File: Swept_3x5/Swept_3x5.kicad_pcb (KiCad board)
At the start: 2 copper layers, 261.1 x 90.7 mm, 98 parts, among them SW10 SW_Push, SW10_r1 SW_Push, SW11 SW_Push, SW11_r1 SW_Push, SW12 SW_Push, SW12_r1 SW_Push, SW13 SW_Push, SW13_r1 SW_Push, SW14 SW_Push, SW14_r1 SW_Push, SW15 SW_Push, SW15_r1 SW_Push, SW16 SW_Push, SW16_r1 SW_Push, SW17 SW_Push, SW17_r1 SW_Push, SW18 SW_Push, SW18_r1 SW_Push, SW19 SW_Push, SW19_r1 SW_Push, SW2 SW_Push, SW20 SW_Push, SW20_r1 SW_Push, SW21 SW_Push, SW21_r1 SW_Push, SW22 SW_Push, SW22_r1 SW_Push, SW2_r1 SW_Push, SW3 SW_Push, SW3_r1 SW_Push, SW4 SW_Push, SW4_r1 SW_Push, SW5 SW_Push, SW5_r1 SW_Push, SW6 SW_Push, SW6_r1 SW_Push, SW7 SW_Push, SW7_r1 SW_Push, SW8 SW_Push, SW8_r1 SW_Push, SW9 SW_Push, SW9_r1 SW_Push, U1 ProMicro-kbd, U2 ProMicro-kbd

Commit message: Version 0.2.0
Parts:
- removed D0, D12, D6, Dr0, Dr12, Dr6: D, kbd:D3_SMD_v2
- removed SW14, SW14_r1, SW2, SW2_r1, SW8, SW8_r1: SW_Push, aym1607:choc-v1-with-millmax
- moved + 34.1 mm to (229.8, 47.6)
- moved - 34.1 mm to (241.9, 47.7)
- moved D1 34.1 mm to (141.8, 42.2)
- moved D10 34.1 mm to (195.7, 45.9)
- moved D13 34.1 mm to (141.8, 76.5)
- moved D14 34.1 mm to (159.7, 64.7)
- moved D15 34.1 mm to (177.8, 57.6)
- moved D16 34.1 mm to (195.7, 63.0)
- moved D18 34.1 mm to (194.5, 92.5)
- moved D19 34.1 mm to (213.2, 94.9)
- moved D2 34.1 mm to (159.8, 30.2)
- moved D3 34.1 mm to (177.8, 23.4)
- moved D4 34.1 mm to (195.8, 28.8)
- moved D7 34.1 mm to (141.6, 59.3)
- moved D8 34.1 mm to (159.8, 47.4)
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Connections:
- U1 pad 20: col0 -> unconnected-(U1-Pad20)
- U2 pad 20: col0r -> unconnected-(U2-Pad20)
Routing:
- net col0r: track 186.0 -> 0.00 mm, vias 3 -> 0
- net col0: track 162.3 -> 0.00 mm, vias 3 -> 0
- net row_2: track 171.9 -> 150.8 mm
- net row_2r: track 135.4 -> 114.8 mm
- net row_1r: track 148.3 -> 127.8 mm
- net row_0r: track 174.3 -> 154.3 mm
- net row_0: track 213.1 -> 193.2 mm
- net row_1: track 188.3 -> 168.5 mm
- net Net-(Dr0-Pad2): track 15.9 -> 0.00 mm
- net Net-(SW8_r1-Pad2): track 15.8 -> 0.00 mm
- net Net-(Dr12-Pad2): track 15.3 -> 0.00 mm
- net Net-(D0-Pad2): track 9.28 -> 0.00 mm
- net Net-(D6-Pad2): track 9.07 -> 0.00 mm
- net Net-(D12-Pad2): track 8.91 -> 0.00 mm
- net Net-(Dr18-Pad2): track 17.3 -> 10.6 mm
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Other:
- board size 261.1 x 90.7 mm -> 227.1 x 91 mm

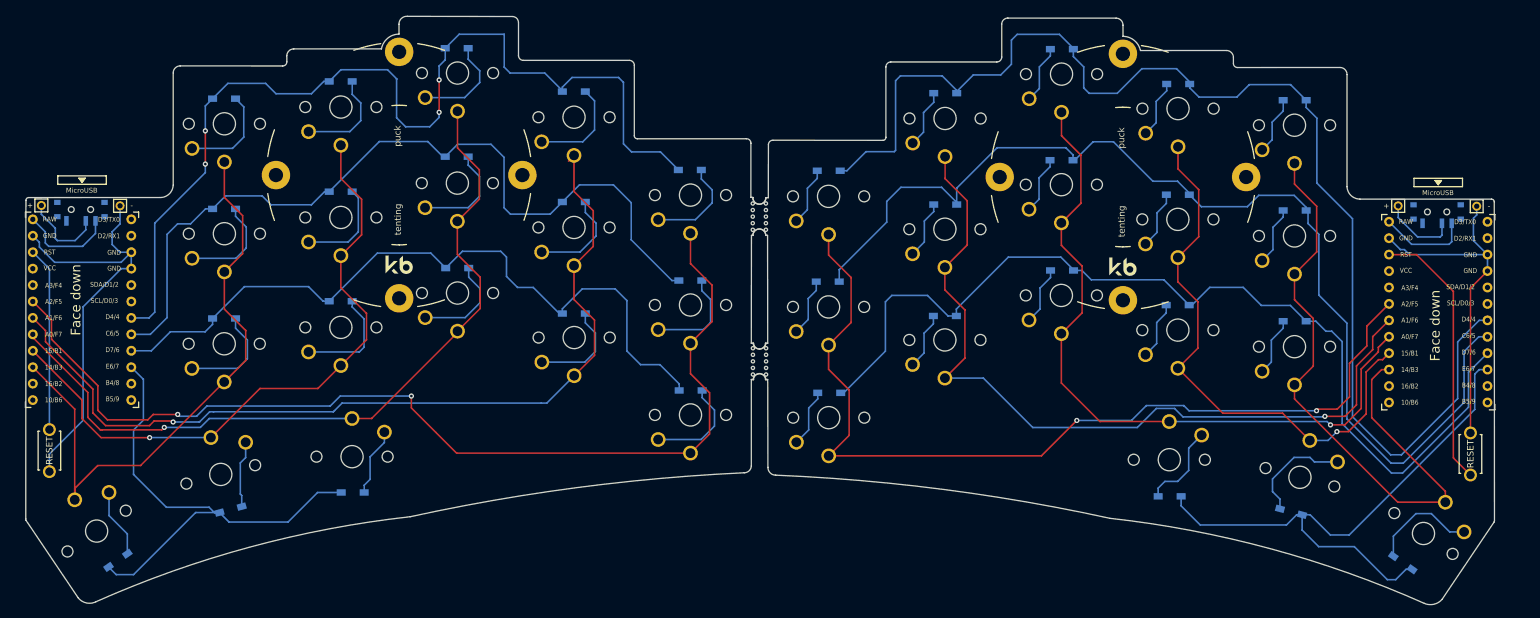
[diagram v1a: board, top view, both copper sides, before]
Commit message: Added support for Kailh hot-swap sockets.
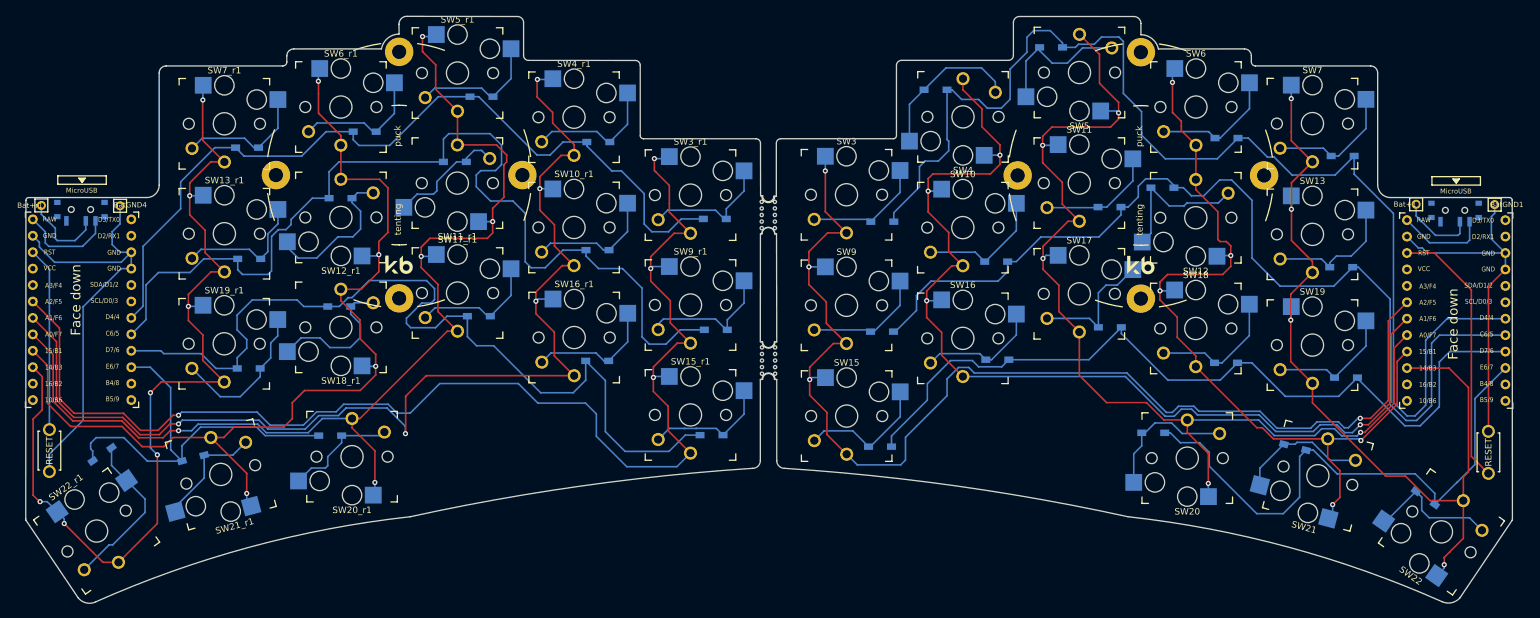
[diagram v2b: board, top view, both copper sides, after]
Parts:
- SW10, SW10_r1, SW11, SW11_r1, SW12, SW12_r1, SW13, SW13_r1, SW15, SW15_r1, SW16, SW16_r1, SW17, SW17_r1, SW18, SW18_r1, SW19, SW19_r1, SW20, SW20_r1, SW21, SW21_r1, SW22, SW22_r1, SW3, SW3_r1, SW4, SW4_r1, SW5, SW5_r1, SW6, SW6_r1, SW7, SW7_r1, SW9, SW9_r1: footprint aym1607:choc-v1-with-millmax -> keyswitches:Kailh_socket_PG1350_optional
- moved Dr20 16.6 mm to (29.4, 86.1)
- moved D8 11.8 mm to (167.7, 56.3)
- moved D17 11.8 mm to (221.7, 74.2)
- moved D16 11.6 mm to (203.2, 71.9)
- moved D15 11.5 mm to (185.2, 66.4)
- moved D13 11.4 mm to (149.7, 84.9)
- moved D1 11.4 mm to (150.1, 50.1)
- moved D7 11.4 mm to (150.0, 67.1)
- moved D5 11.4 mm to (221.2, 39.9)
- moved D11 11.3 mm to (221.0, 57.1)
- moved D4 11.2 mm to (203.3, 37.2)
- moved D20 10.6 mm to (234.0, 92.8)
- moved D14 10.6 mm to (167.8, 71.4)
- moved D9 10.4 mm to (185.2, 47.8)
- moved D18 10.1 mm to (191.9, 82.7)
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- renumbered + to Bat+1, + to Bat+r1, - to BatGND1, - to BatGND4
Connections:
- U1 pad 20: unconnected-(U1-Pad20) -> col0
- U2 pad 20: unconnected-(U2-Pad20) -> col0r
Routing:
- net col3: track 110.0 -> 161.3 mm, vias 1 -> 5
- net col3r: track 121.2 -> 172.3 mm, vias 1 -> 5
- net col4r: track 99.5 -> 149.1 mm, vias 1 -> 4
- net col5r: track 94.0 -> 143.4 mm, vias 0 -> 7
- net col4: track 86.1 -> 127.7 mm, vias 1 -> 5
- net col1: track 141.6 -> 182.8 mm, vias 2 -> 4
- net col1r: track 158.9 -> 198.7 mm, vias 2 -> 4
- net col2r: track 137.4 -> 175.6 mm, vias 1 -> 5
- net col2: track 124.6 -> 160.5 mm, vias 1 -> 4
- net col5: track 98.6 -> 131.6 mm, vias 0 -> 4
- net row_0r: track 154.3 -> 128.3 mm, vias 4 -> 0
- net row_2: track 150.8 -> 126.1 mm
- net row_1r: track 127.8 -> 152.2 mm
- net row_2r: track 114.8 -> 137.5 mm
- net Net-(D2-Pad2): track 9.06 -> 23.8 mm
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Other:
- board size 227.1 x 91 mm -> 229.8 x 90.7 mm

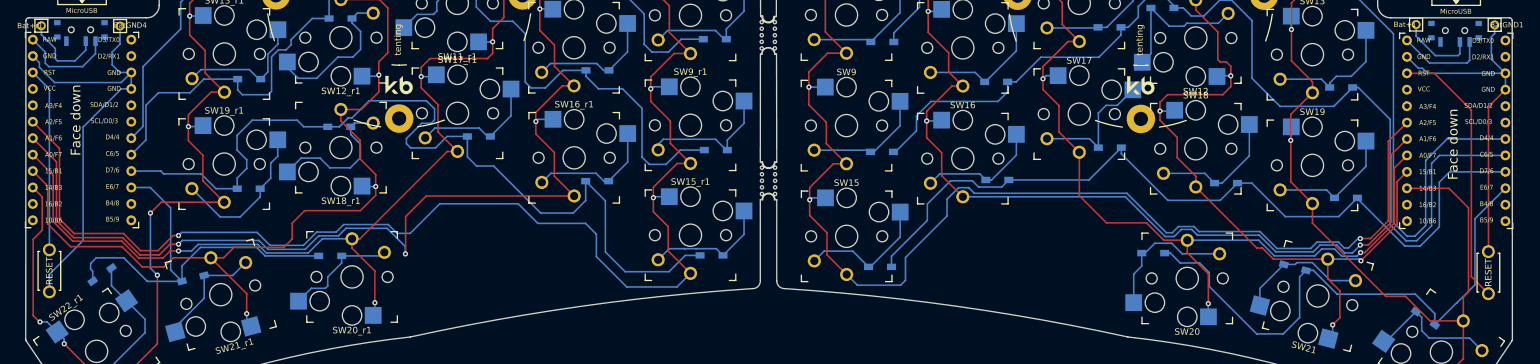
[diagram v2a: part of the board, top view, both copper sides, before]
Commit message: Added nice!view support for 3x5
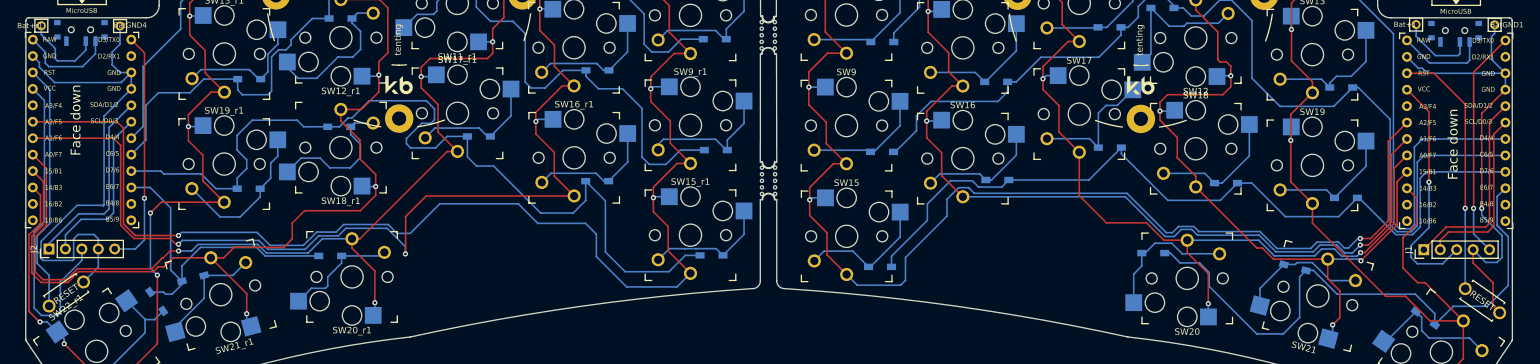
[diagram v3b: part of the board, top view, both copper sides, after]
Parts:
- added J1: ScreenL, Connector_PinHeader_2.54mm:PinHeader_1x05_P2.54mm_Vertical, F.Cu at (233.8, 82.2)
- added J2: ScreenR, Connector_PinHeader_2.54mm:PinHeader_1x05_P2.54mm_Vertical, F.Cu at (21.2, 82.1)
- moved Dr20 9.40 mm to (37.9, 90.2), turned to -55 degrees
- moved RSW1 4.44 mm to (242.8, 90.1), turned to -35 degrees
- moved RSW2 4.43 mm to (23.9, 89.0), turned to 35 degrees
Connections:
- U1 pad 1: unconnected-(U1-Pad1) -> CS
- U1 pad 5: unconnected-(U1-Pad5) -> MOSI
- U1 pad 6: unconnected-(U1-Pad6) -> SCK
- U2 pad 1: unconnected-(U2-Pad1) -> CSr
- U2 pad 5: unconnected-(U2-Pad5) -> MOSIr
- U2 pad 6: unconnected-(U2-Pad6) -> SCKr
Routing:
- net vcc_r: track 0.00 -> 51.2 mm
- net CSr: track 0.00 -> 37.0 mm, vias 0 -> 1
- net vcc: track 0.00 -> 36.9 mm, vias 0 -> 1
- net CS: track 0.00 -> 35.4 mm, vias 0 -> 1
- net MOSI: track 0.00 -> 31.0 mm
- net MOSIr: track 0.00 -> 29.8 mm
- net SCK: track 0.00 -> 27.4 mm
- net SCKr: track 0.00 -> 26.2 mm
- net gnd: track 53.5 -> 73.2 mm, vias 0 -> 1
- net gnd_r: track 68.0 -> 85.4 mm
- net row_3r: track 63.6 -> 50.9 mm
- net col3r: track 172.3 -> 182.6 mm
- net reset_r: track 28.5 -> 38.8 mm
- net col4r: track 149.1 -> 158.5 mm
- net row_3: track 86.1 -> 90.6 mm
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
